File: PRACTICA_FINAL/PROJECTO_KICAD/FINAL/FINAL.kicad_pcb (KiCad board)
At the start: 4 copper layers, 100 x 56 mm, 115 parts, among them IC1 FT2232H, SW1 SWITCH-2CH-6P-3010010P1, SW2 EVQQ2, U1 ARDUINO_MEGA_SHIELD, U101 ATMEGA32U4-XUMU, U2 LTC3419MS, U3 93C56B, X1 12MHz, Y1 16Mhz KX-7

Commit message: Se conecta la señal de JTAG_REG del conector JTAG estaba conectado en el PCB y en el esquematico no se vio conectado. Se hace la modificacion en el esquematico y se hace backannotate al PCB:
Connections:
- U$1 pad JTAG_REF: Net-(U$1-PadJTAG_REF) -> +3V3
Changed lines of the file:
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@@
     (zones 0)
     (modules 115)
-    (nets 214)
+    (nets 213)
   )
   (page A4)
@@
     (35 F.Paste user hide)
     (36 B.SilkS user hide)
-    (37 F.SilkS user hide)
+    (37 F.SilkS user)
     (38 B.Mask user hide)
     (39 F.Mask user hide)
@@
   (net 205 /Arduino/ATMEGA_D2)
   (net 206 "Net-(U$1-PadJTAG_GND)")
-  (net 207 "Net-(U$1-PadJTAG_REF)")
-  (net 208 "Net-(WING_POWER1-PadP2)")
-  (net 209 "Net-(WING_POWER2-PadP2)")
-  (net 210 "Net-(WING_POWER3-PadP2)")
-  (net 211 "Net-(WING_POWER4-PadP2)")
-  (net 212 "Net-(WING_POWER5-PadP2)")
-  (net 213 "Net-(WING_POWER6-PadP2)")
+  (net 207 "Net-(WING_POWER1-PadP2)")
+  (net 208 "Net-(WING_POWER2-PadP2)")
+  (net 209 "Net-(WING_POWER3-PadP2)")
+  (net 210 "Net-(WING_POWER4-PadP2)")
+  (net 211 "Net-(WING_POWER5-PadP2)")
+  (net 212 "Net-(WING_POWER6-PadP2)")
   (net_class Default "Esta es la clase de red por defecto."
     (clearance 0.2)
@@
     (add_net "Net-(SW1-PadCOM1)")
     (add_net "Net-(U$1-PadJTAG_GND)")
-    (add_net "Net-(U$1-PadJTAG_REF)")
     (add_net "Net-(U1-PadVIN)")
     (add_net "Net-(U101-Pad22)")
@@
       (net 6 +3V3) (solder_mask_margin 0.0508))
     (pad P2 thru_hole circle (at 0 -1.27 180) (size 1.308 1.308) (drill 0.8) (layers *.Cu *.Mask)
-      (net 211 "Net-(WING_POWER4-PadP2)") (solder_mask_margin 0.0508))
+      (net 210 "Net-(WING_POWER4-PadP2)") (solder_mask_margin 0.0508))
     (pad P1 thru_hole rect (at 0 -3.81 180) (size 1.308 1.308) (drill 0.8) (layers *.Cu *.Mask)
       (net 5 GND) (solder_mask_margin 0.0508))
@@
       (net 206 "Net-(U$1-PadJTAG_GND)") (solder_mask_margin 0.0508))
     (pad JTAG_REF thru_hole rect (at 12.7 0 90) (size 1.524 1.524) (drill 1.016) (layers *.Cu *.Mask)
-      (net 207 "Net-(U$1-PadJTAG_REF)") (solder_mask_margin 0.0508))
+      (net 6 +3V3) (solder_mask_margin 0.0508))
     (pad JTAG_TCK thru_hole circle (at 7.62 0 90) (size 1.524 1.524) (drill 1.016) (layers *.Cu *.Mask)
       (net 63 /FPGA/AD0-JTAG_TCK) (solder_mask_margin 0.0508))
@@
       (net 6 +3V3) (solder_mask_margin 0.0508))
     (pad P2 thru_hole circle (at 0 -1.27 180) (size 1.308 1.308) (drill 0.8) (layers *.Cu *.Mask)
-      (net 208 "Net-(WING_POWER1-PadP2)") (solder_mask_margin 0.0508))
+      (net 207 "Net-(WING_POWER1-PadP2)") (solder_mask_margin 0.0508))
     (pad P1 thru_hole rect (at 0 -3.81 180) (size 1.308 1.308) (drill 0.8) (layers *.Cu *.Mask)
       (net 5 GND) (solder_mask_margin 0.0508))
@@
       (net 6 +3V3) (solder_mask_margin 0.0508))
     (pad P2 thru_hole circle (at 0 -1.27 270) (size 1.308 1.308) (drill 0.8) (layers *.Cu *.Mask)
-      (net 209 "Net-(WING_POWER2-PadP2)") (solder_mask_margin 0.0508))
+      (net 208 "Net-(WING_POWER2-PadP2)") (solder_mask_margin 0.0508))
     (pad P1 thru_hole rect (at 0 -3.81 270) (size 1.308 1.308) (drill 0.8) (layers *.Cu *.Mask)
       (net 5 GND) (solder_mask_margin 0.0508))
@@
       (net 6 +3V3) (solder_mask_margin 0.0508))
     (pad P2 thru_hole circle (at 0 -1.27 90) (size 1.308 1.308) (drill 0.8) (layers *.Cu *.Mask)
-      (net 210 "Net-(WING_POWER3-PadP2)") (solder_mask_margin 0.0508))
+      (net 209 "Net-(WING_POWER3-PadP2)") (solder_mask_margin 0.0508))
     (pad P1 thru_hole rect (at 0 -3.81 90) (size 1.308 1.308) (drill 0.8) (layers *.Cu *.Mask)
       (net 5 GND) (solder_mask_margin 0.0508))
@@
       (net 6 +3V3) (solder_mask_margin 0.0508))
     (pad P2 thru_hole circle (at 0 -1.27 270) (size 1.308 1.308) (drill 0.8) (layers *.Cu *.Mask)
-      (net 212 "Net-(WING_POWER5-PadP2)") (solder_mask_margin 0.0508))
+      (net 211 "Net-(WING_POWER5-PadP2)") (solder_mask_margin 0.0508))
     (pad P1 thru_hole rect (at 0 -3.81 270) (size 1.308 1.308) (drill 0.8) (layers *.Cu *.Mask)
       (net 5 GND) (solder_mask_margin 0.0508))
@@
       (net 6 +3V3) (solder_mask_margin 0.0508))
     (pad P2 thru_hole circle (at 0 -1.27 270) (size 1.308 1.308) (drill 0.8) (layers *.Cu *.Mask)
-      (net 213 "Net-(WING_POWER6-PadP2)") (solder_mask_margin 0.0508))
+      (net 212 "Net-(WING_POWER6-PadP2)") (solder_mask_margin 0.0508))
     (pad P1 thru_hole rect (at 0 -3.81 270) (size 1.308 1.308) (drill 0.8) (layers *.Cu *.Mask)
       (net 5 GND) (solder_mask_margin 0.0508))

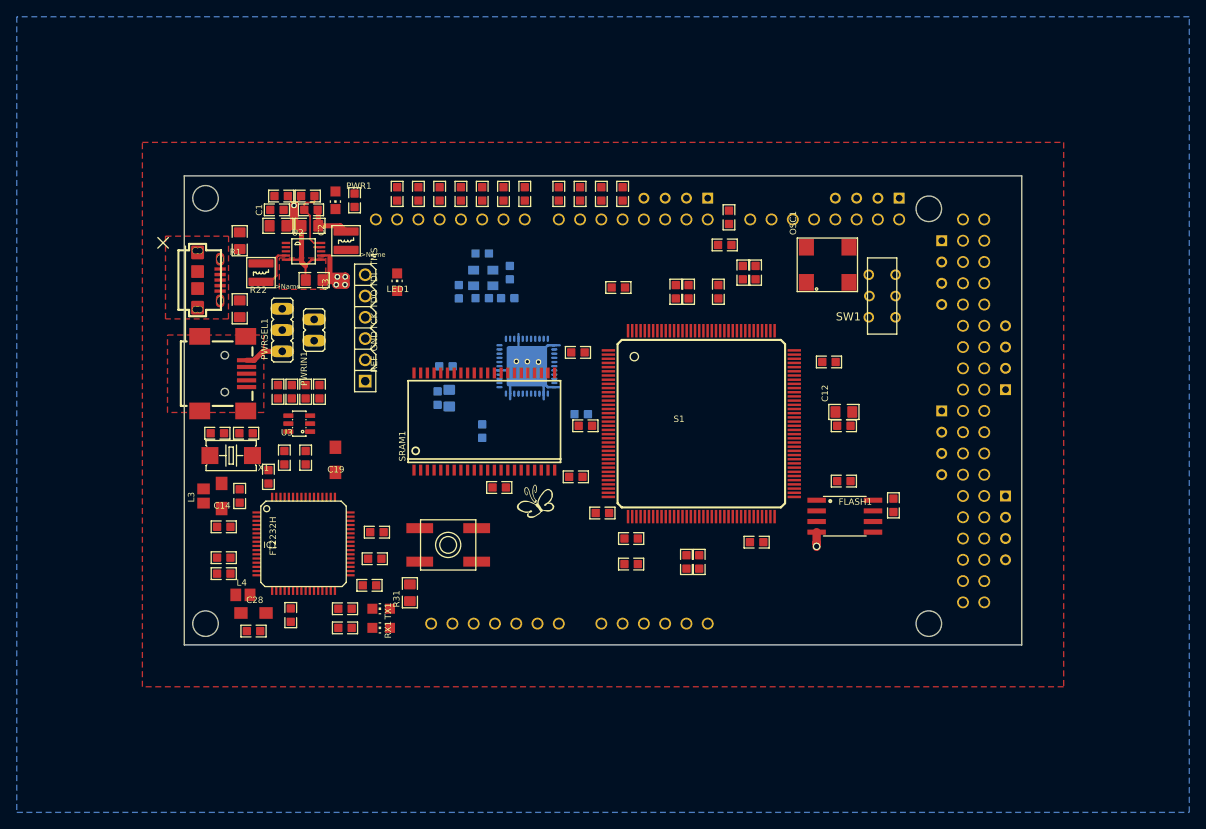
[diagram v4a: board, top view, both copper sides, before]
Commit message: Se agrega Logos y Simbolos Se agrega fiduciales Se acomoda serigrafia para que sea visible y coherente Se agrega libreria de giduciales Se crea simbolo para el logo
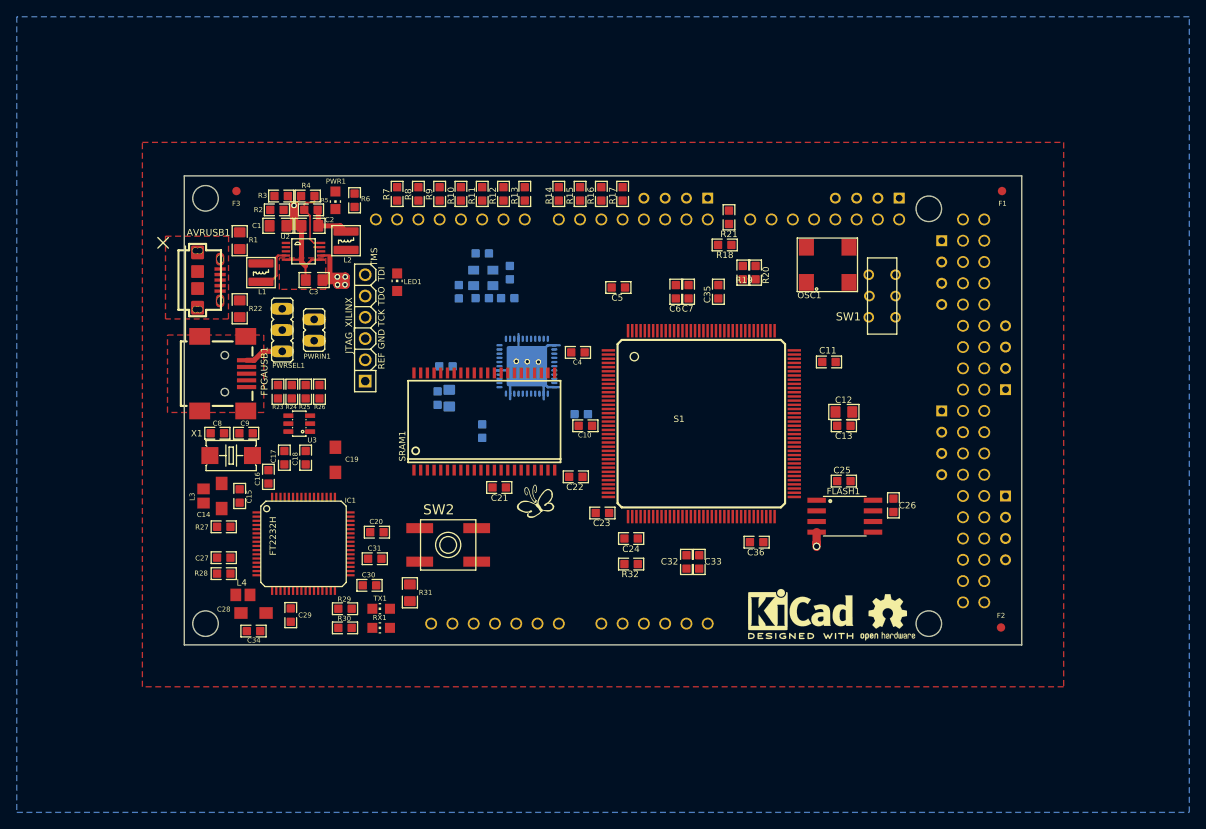
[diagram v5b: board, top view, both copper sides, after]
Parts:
- added F1: Fiducial, Fiducial:Fiducial_1mm_Dia_2mm_Outer, F.Cu at (196.1, 78.8)
- added F2: Fiducial, Fiducial:Fiducial_1mm_Dia_2mm_Outer, F.Cu at (196.0, 130.9)
- added F3: Fiducial, Fiducial:Fiducial_1mm_Dia_2mm_Outer, F.Cu at (104.7, 78.8)
- added LOGO1: Logo_Open_Hardware_Small, Symbol:OSHW-Logo2_7.3x6mm_SilkScreen, F.Cu at (182.5, 129.7)
- added LOGO2: logo_glavigna, Symbol:KiCad-Logo2_6mm_SilkScreen, F.Cu at (172.1, 129.3)

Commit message: Se actualizan correcciones en el PCB
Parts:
- moved LOGO1 3.20 mm to (181.4, 126.7)
- moved LOGO2 2.97 mm to (171.1, 126.5)
- moved R18 0.67 mm to (163.7, 85.3)
- turned OSC1 to 270 degrees
- turned SRAM1 to 180 degrees
- renumbered SW2 to RESET
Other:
- board text added: "JLCPCB Fab ****************************** Paste Mask White ------------------------- Silkscreen Top White ------------------------- Solder Mask Top Green ------------------------- Top 1 Oz HASL ------------------------- Prepreg 4 mils ------------------------- Route 2 0.5 Oz ------------------------- Core FR4 50 mil ------------------------- Route 3 0.5 Oz ------------------------- Prepreg 4 mils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"
- board text added: "Papilio Platform Papilio Duo Clone Gonzalo Lavigna 2018/11/17 V1.1"
- board text added: "W1"
- board text added: "W2"
- board text added: "W3"
- board text added: "W4"
- board text added: "W5"
- board text added: "W6"
- board text added: "https://github.com/gonzalolavigna /CESE-2018-disenio-pcb-gonzalo-lavigna"
